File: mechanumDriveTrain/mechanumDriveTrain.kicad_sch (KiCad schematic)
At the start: 38 parts, among them IC1 TCAN3414DR, J1 XT30U-M, J2 BM02B-SRSS-TB, J3 5 pin dupont, J4 5 pin dupont, U1 Teensy 4.1, U2 LD1117S50TR_SOT223

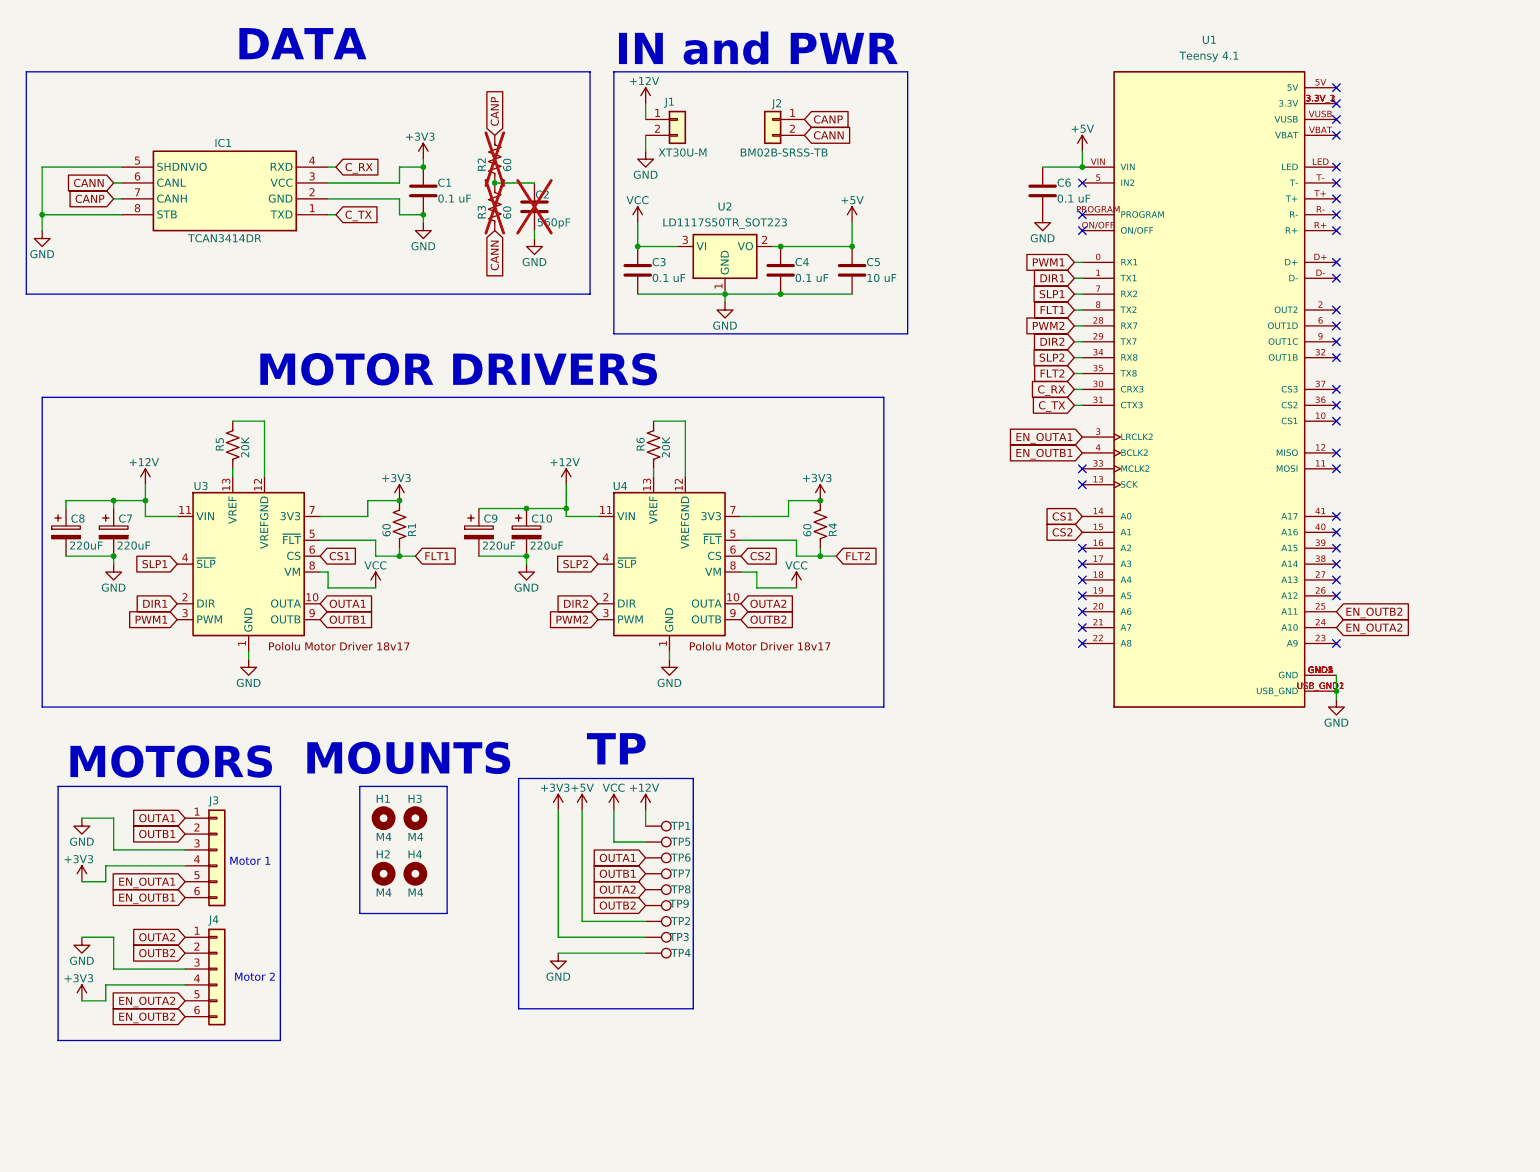
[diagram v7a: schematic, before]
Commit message: Updated board size and layout
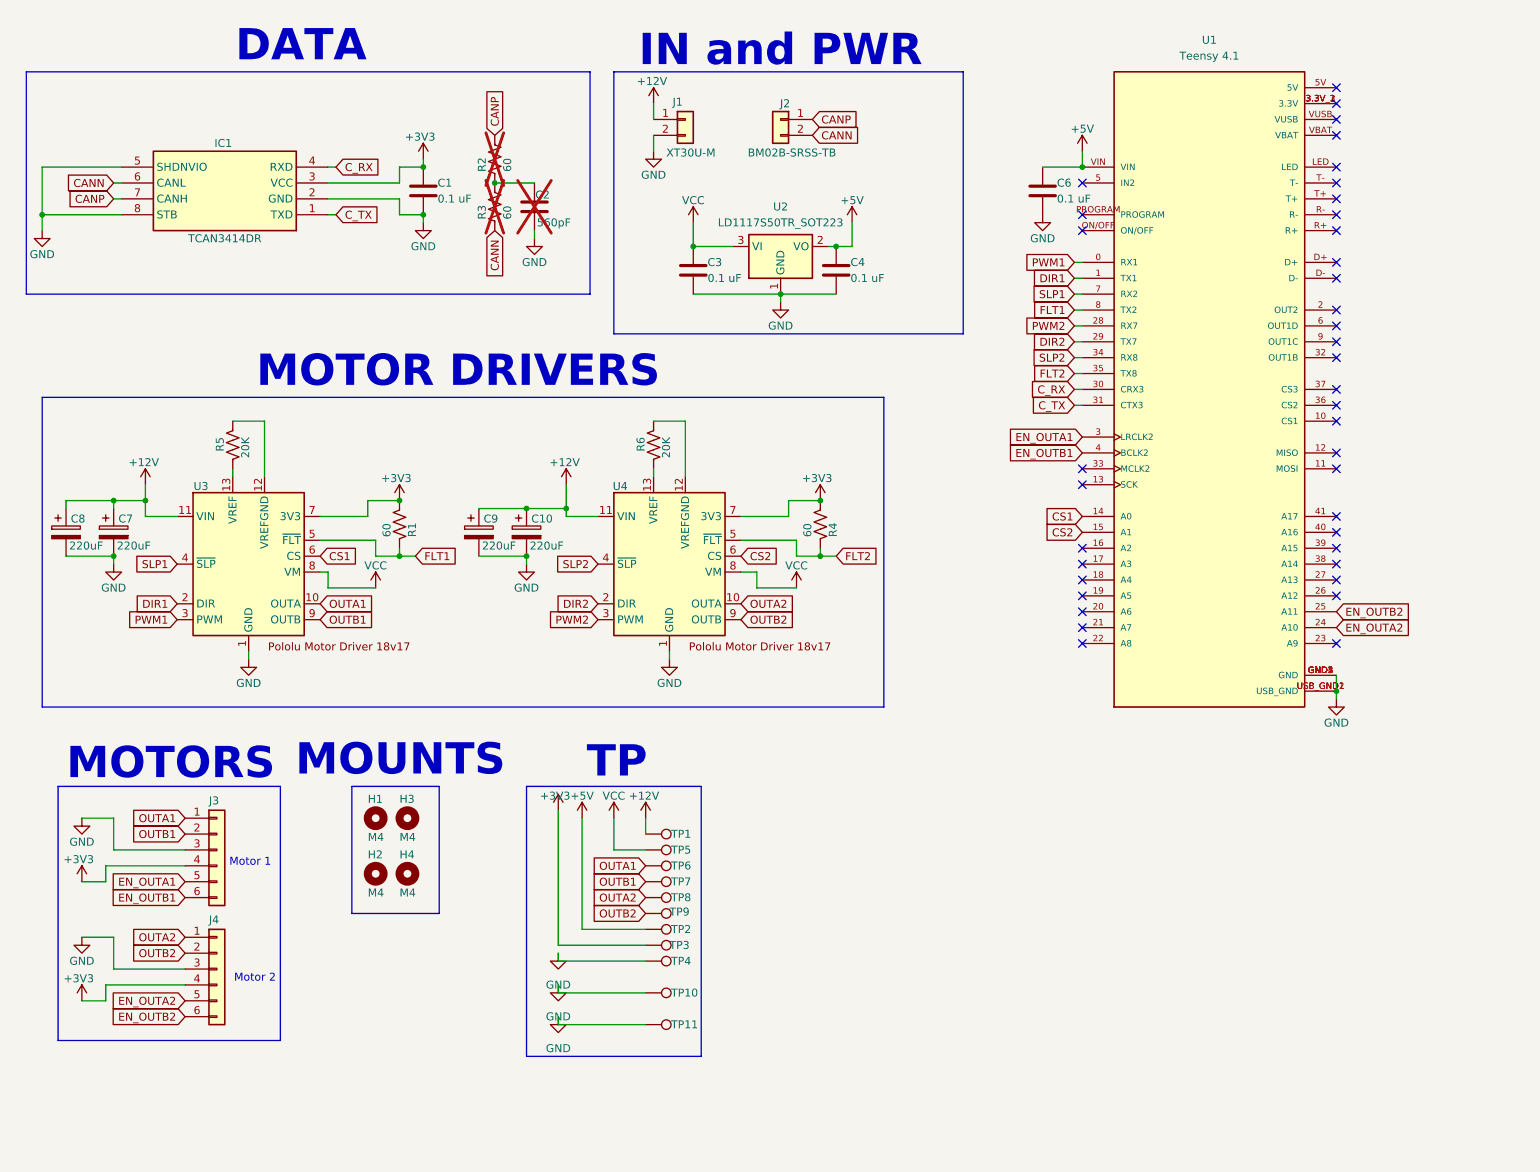
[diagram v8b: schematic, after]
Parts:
- removed C5: 10 uF, Capacitor_SMD:C_0805_2012Metric_Pad1.18x1.45mm_HandSolder, symbol Device:C
- added TP10, TP11: ~, TestPoint:TestPoint_Loop_D1.80mm_Drill1.0mm_Beaded, symbol Connector:TestPoint
- R5, R6: footprint Resistor_SMD:R_0805_2012Metric_Pad1.20x1.40mm_HandSolder -> Resistor_THT:R_Axial_DIN0207_L6.3mm_D2.5mm_P5.08mm_Vertical
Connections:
- net GND: now also TP10.1, TP11.1
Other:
- moved on the sheet: C3, C4, H1, H2, H3, H4, J1, J2, TP1, TP2, TP3, TP4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
